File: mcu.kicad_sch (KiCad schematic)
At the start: 31 parts, among them Q22 Q_NPN_BCE, Q23 Q_NPN_BCE, Q24 Q_NPN_BCE, Q25 Q_NPN_BCE, Q26 Q_NPN_BCE, U2 CH32V103C8T6, U3 XTSD01G, Y1 32.768kHz, Y2 16MHz

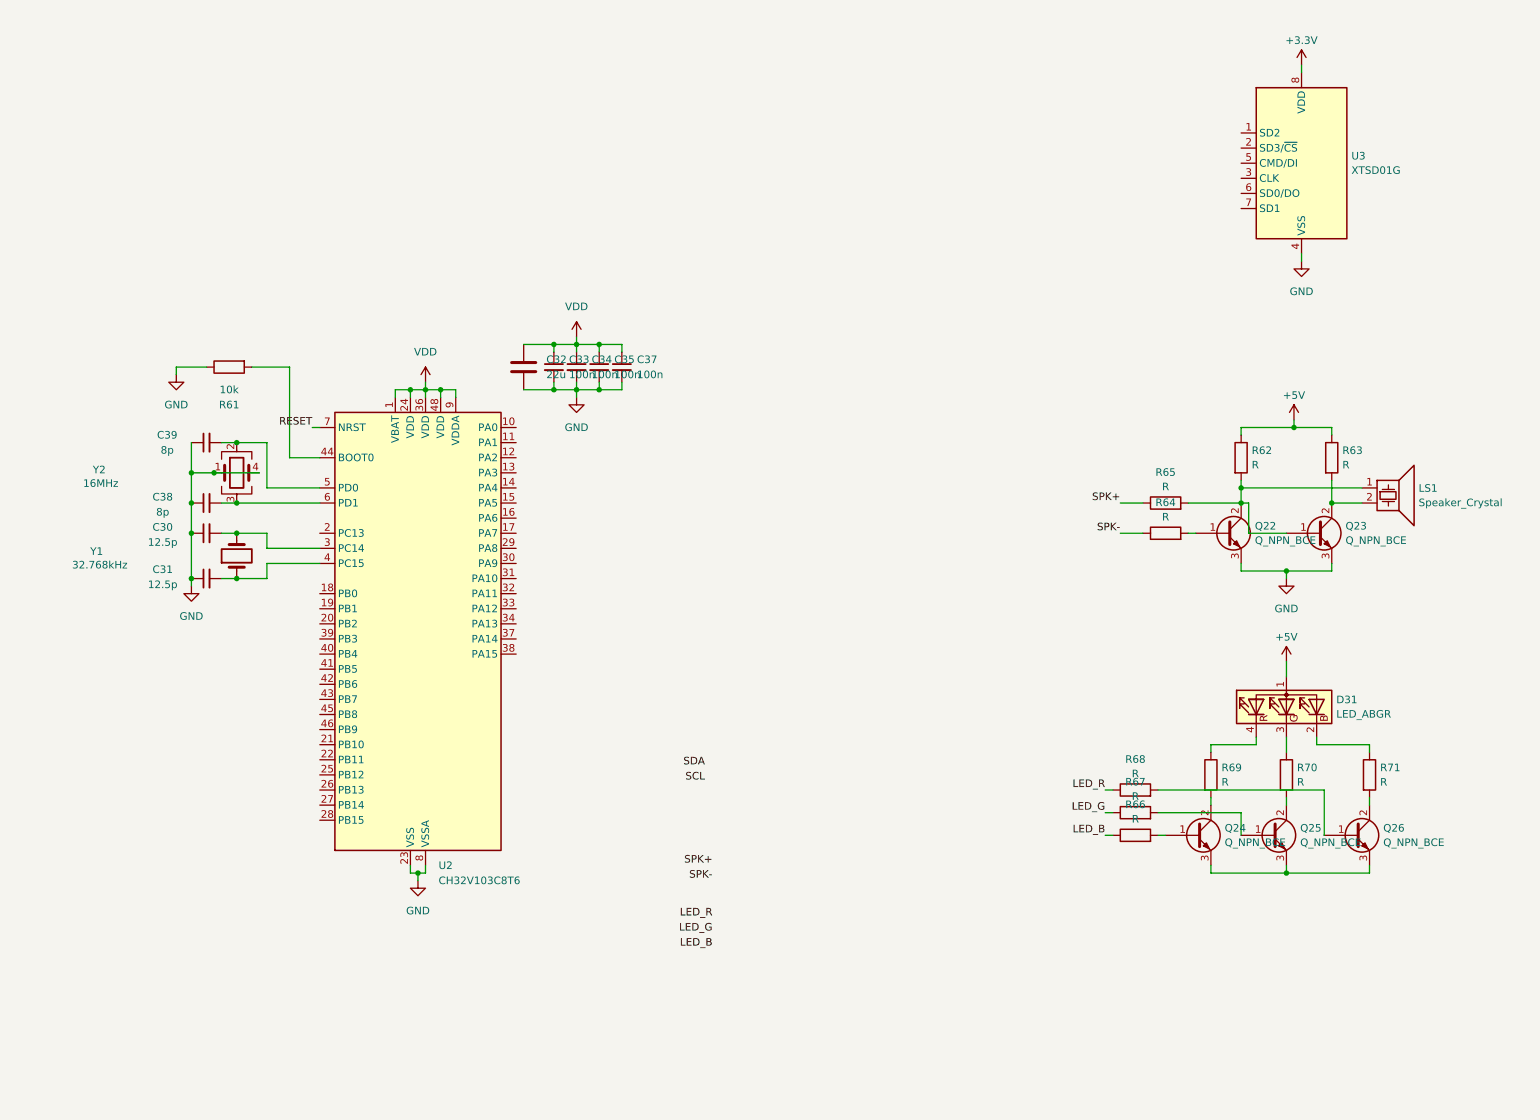
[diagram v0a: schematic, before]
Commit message: fix: 修复commit `38e8c9e`将元器件移动子原理图到造成的位号混乱
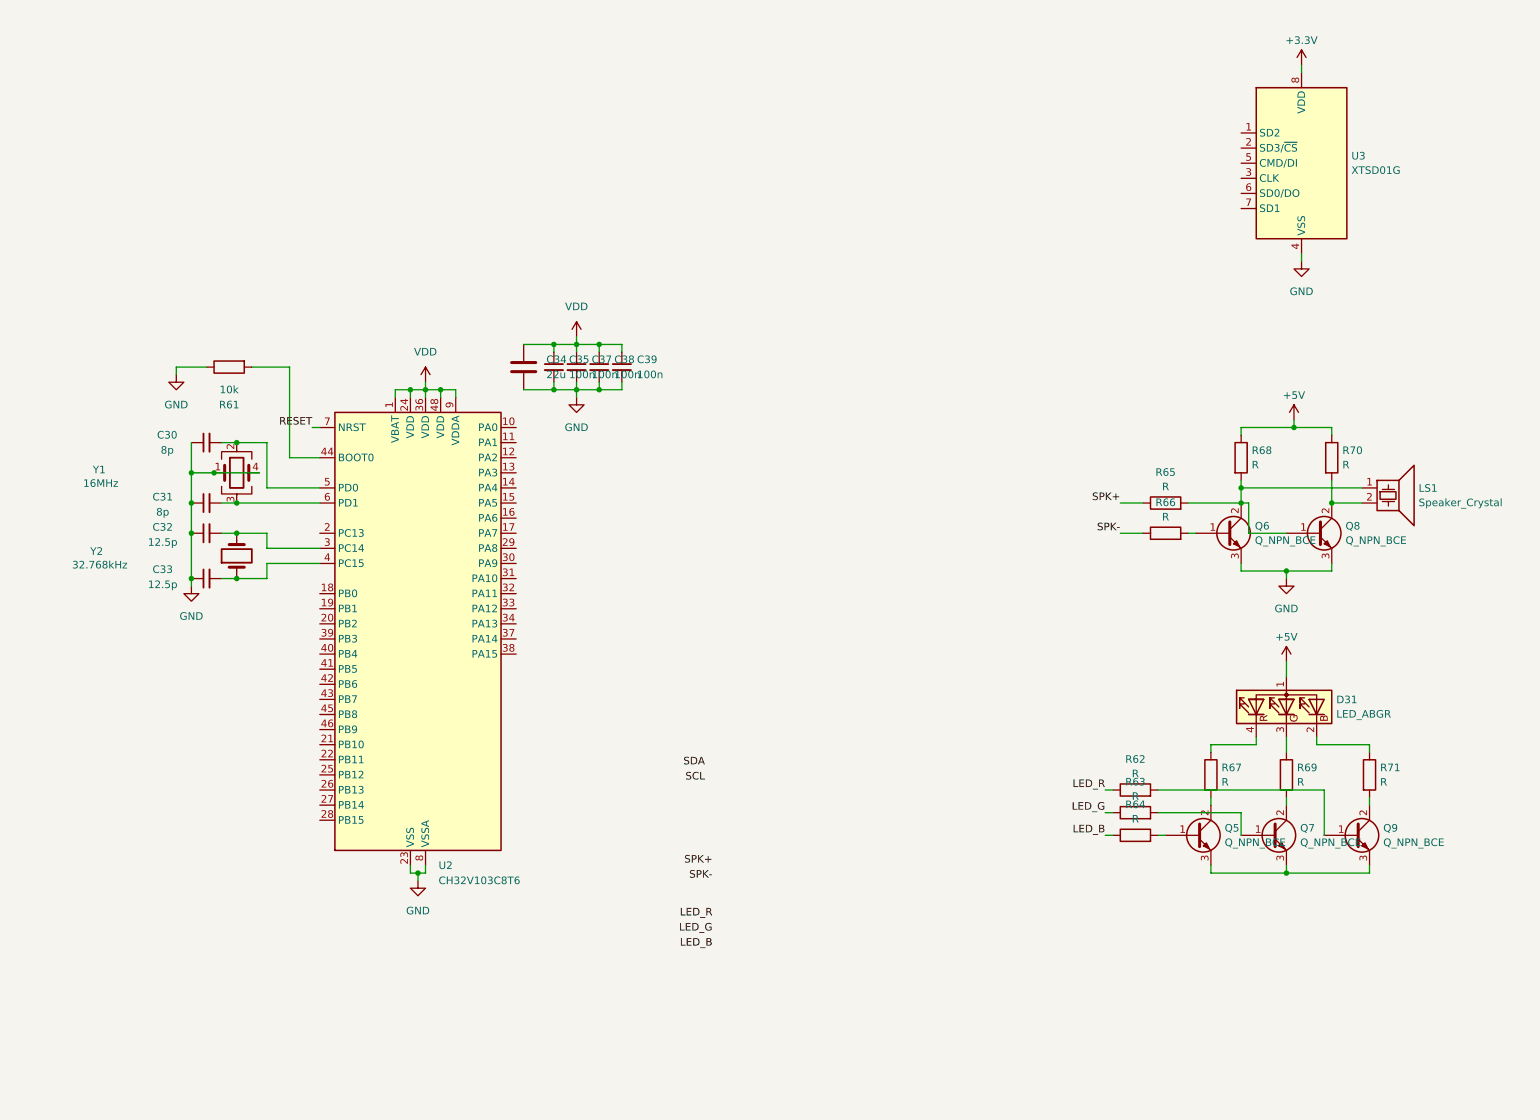
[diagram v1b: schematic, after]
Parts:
- U2: footprint Library:QFP-48_7x7_Pitch0.5mm -> Package_QFP:LQFP-48_7x7mm_P0.5mm
- renumbered C39 to C30, C38 to C31, C30 to C32, C31 to C33, C32 to C34, C33 to C35, C34 to C37, C35 to C38, C37 to C39, Q24 to Q5, Q22 to Q6, Q25 to Q7, Q23 to Q8, Q26 to Q9, R68 to R62, R67 to R63, R66 to R64, R64 to R66, R69 to R67, R62 to R68, R70 to R69, R63 to R70, Y2 to Y1, Y1 to Y2

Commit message: 分配MCU引脚，连接原理图，添加CAN收发器
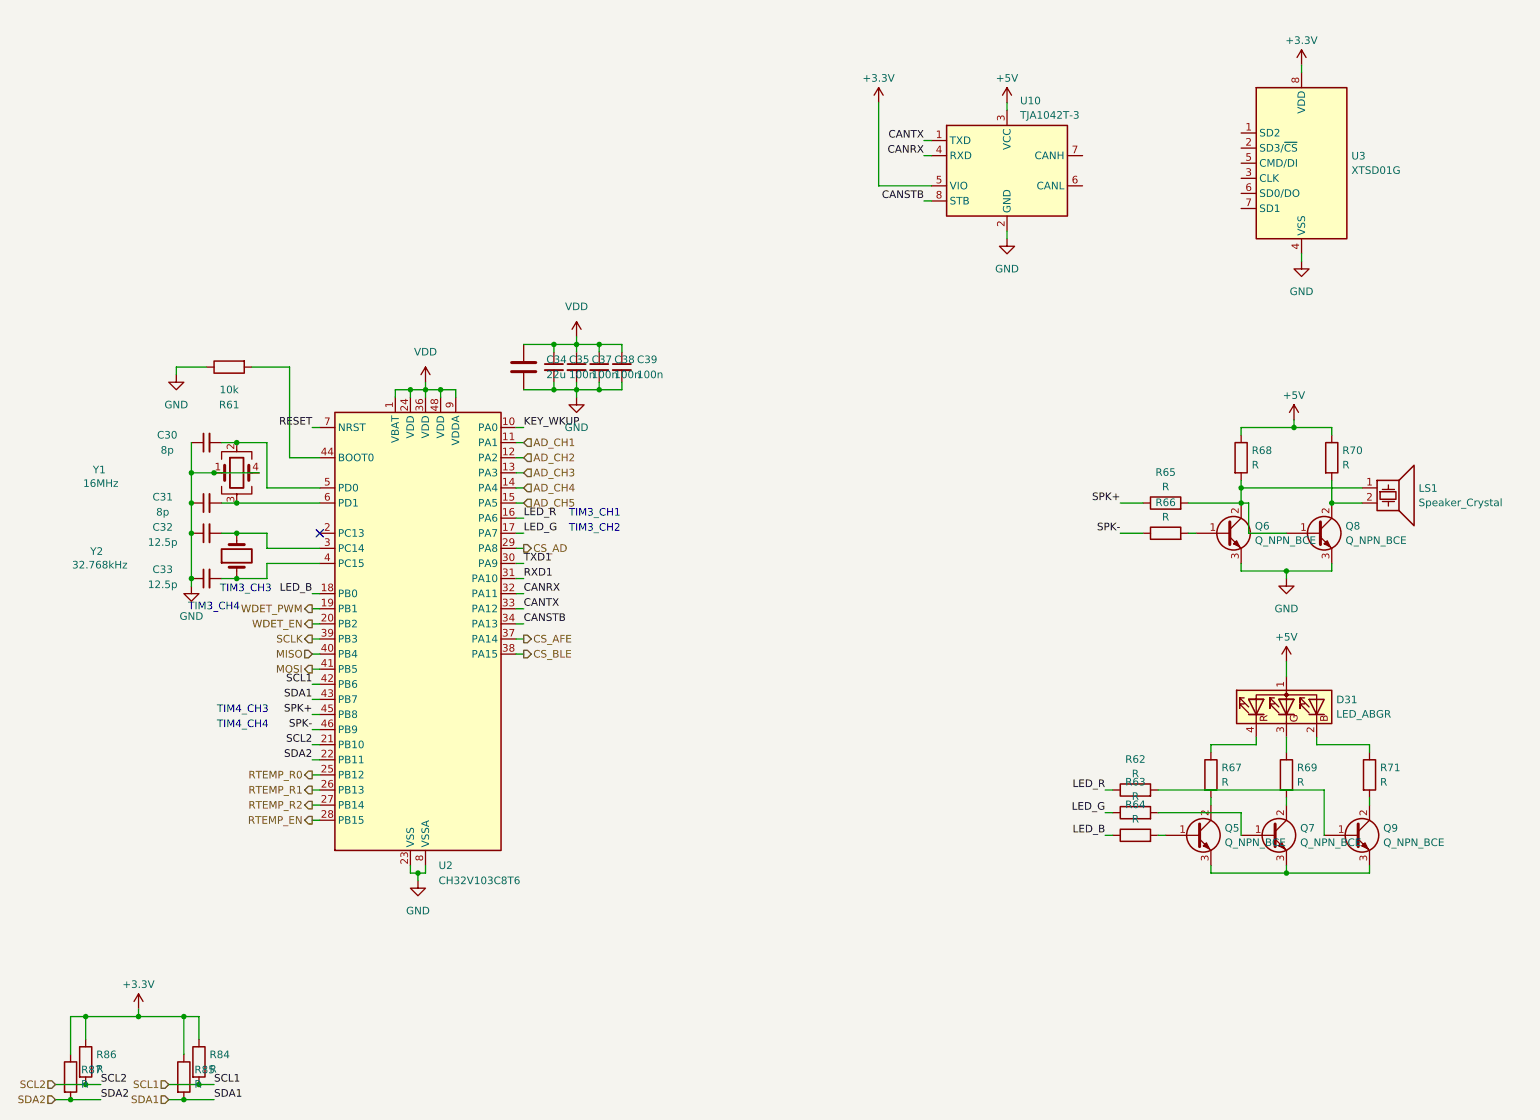
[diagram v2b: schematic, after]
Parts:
- added R84, R85, R86, R87: R, symbol Device:R
- added U10: TJA1042T-3, Package_SO:SOIC-8_3.9x4.9mm_P1.27mm, symbol Interface_CAN_LIN:TJA1042T-3
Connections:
- net +3.3V: now also R84.1, R85.1, R86.1, R87.1, U10.5 (VIO)
- net +5V: now also U10.3 (VCC)
- net GND: now also U10.2 (GND)
- net LED_B: now also U2.18 (PB0)
- net LED_G: now also U2.17 (PA7)
- net LED_R: now also U2.16 (PA6)
- net SPK+: now also U2.45 (PB8)
- net SPK-: now also U2.46 (PB9)
- net KEY_WKUP: now reaches U2.10 (PA0)
- net AD_CH1: now reaches U2.11 (PA1)
- net AD_CH2: now reaches U2.12 (PA2)
- net AD_CH3: now reaches U2.13 (PA3)
- net AD_CH4: now reaches U2.14 (PA4)
- net AD_CH5: now reaches U2.15 (PA5)
- net WDET_PWM: now reaches U2.19 (PB1)
- net WDET_EN: now reaches U2.20 (PB2)
- net SCL2: now reaches U2.21 (PB10)
- net SCL2: now also R86.2
- net SDA2: now reaches U2.22 (PB11)
- net SDA2: now also R87.2
- net RTEMP_R0: now reaches U2.25 (PB12)
- net RTEMP_R1: now reaches U2.26 (PB13)
- net RTEMP_R2: now reaches U2.27 (PB14)
- net RTEMP_EN: now reaches U2.28 (PB15)
- net CS_AD: now reaches U2.29 (PA8)
- net TXD1: now reaches U2.30 (PA9)
- net RXD1: now reaches U2.31 (PA10)
- net CANRX: now reaches U2.32 (PA11)
- net CANRX: now also U10.4 (RXD)
- net CANTX: now reaches U2.33 (PA12)
- net CANTX: now also U10.1 (TXD)
- net CANSTB: now reaches U2.34 (PA13)
- net CANSTB: now also U10.8 (STB)
- net CS_AFE: now reaches U2.37 (PA14)
- net CS_BLE: now reaches U2.38 (PA15)
- net SCLK: now reaches U2.39 (PB3)
- net MISO: now reaches U2.40 (PB4)
- net MOSI: now reaches U2.41 (PB5)
- net SCL1: now reaches U2.42 (PB6)
- net SCL1: now also R84.2
- net SDA1: now reaches U2.43 (PB7)
- net SDA1: now also R85.2
- no-connect marks 0 -> 1
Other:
- note added: "TIM3_CH1"
- note added: "TIM3_CH2"
- note added: "TIM3_CH3"
- note added: "TIM3_CH4"
- note added: "TIM4_CH3"
- note added: "TIM4_CH4"

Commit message: AFE改为PB7170(LQFP-64)，修改原理图，调整元器件布局
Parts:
- R61: footprint Resistor_SMD:R_0201_0603Metric -> Resistor_SMD:R_0402_1005Metric
- Y1: symbol Device:Crystal_GND23 -> Device:Crystal_GND24
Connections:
- net GND: now also Y1.3; no longer Y1.4
- net at C31.2, U2.6 (PD1): now also Y1.4; no longer Y1.3
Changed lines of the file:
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@@
 			)
 		)
-		(property "Footprint" "Resistor_SMD:R_0201_0603Metric"
+		(property "Footprint" "Resistor_SMD:R_0402_1005Metric"
 			(at 50.8 69.342 90)
 			(effects
@@
 	)
 	(symbol
-		(lib_id "Device:Crystal_GND23")
+		(lib_id "Device:Crystal_GND24")
 		(at 52.07 88.9 0)
 		(unit 1)
@@
 			)
 		)
-		(property "Description" "Four pin crystal, GND on pins 2 and 3"
+		(property "Description" "Four pin crystal, GND on pins 2 and 4"
 			(at 52.07 88.9 0)
 			(effects

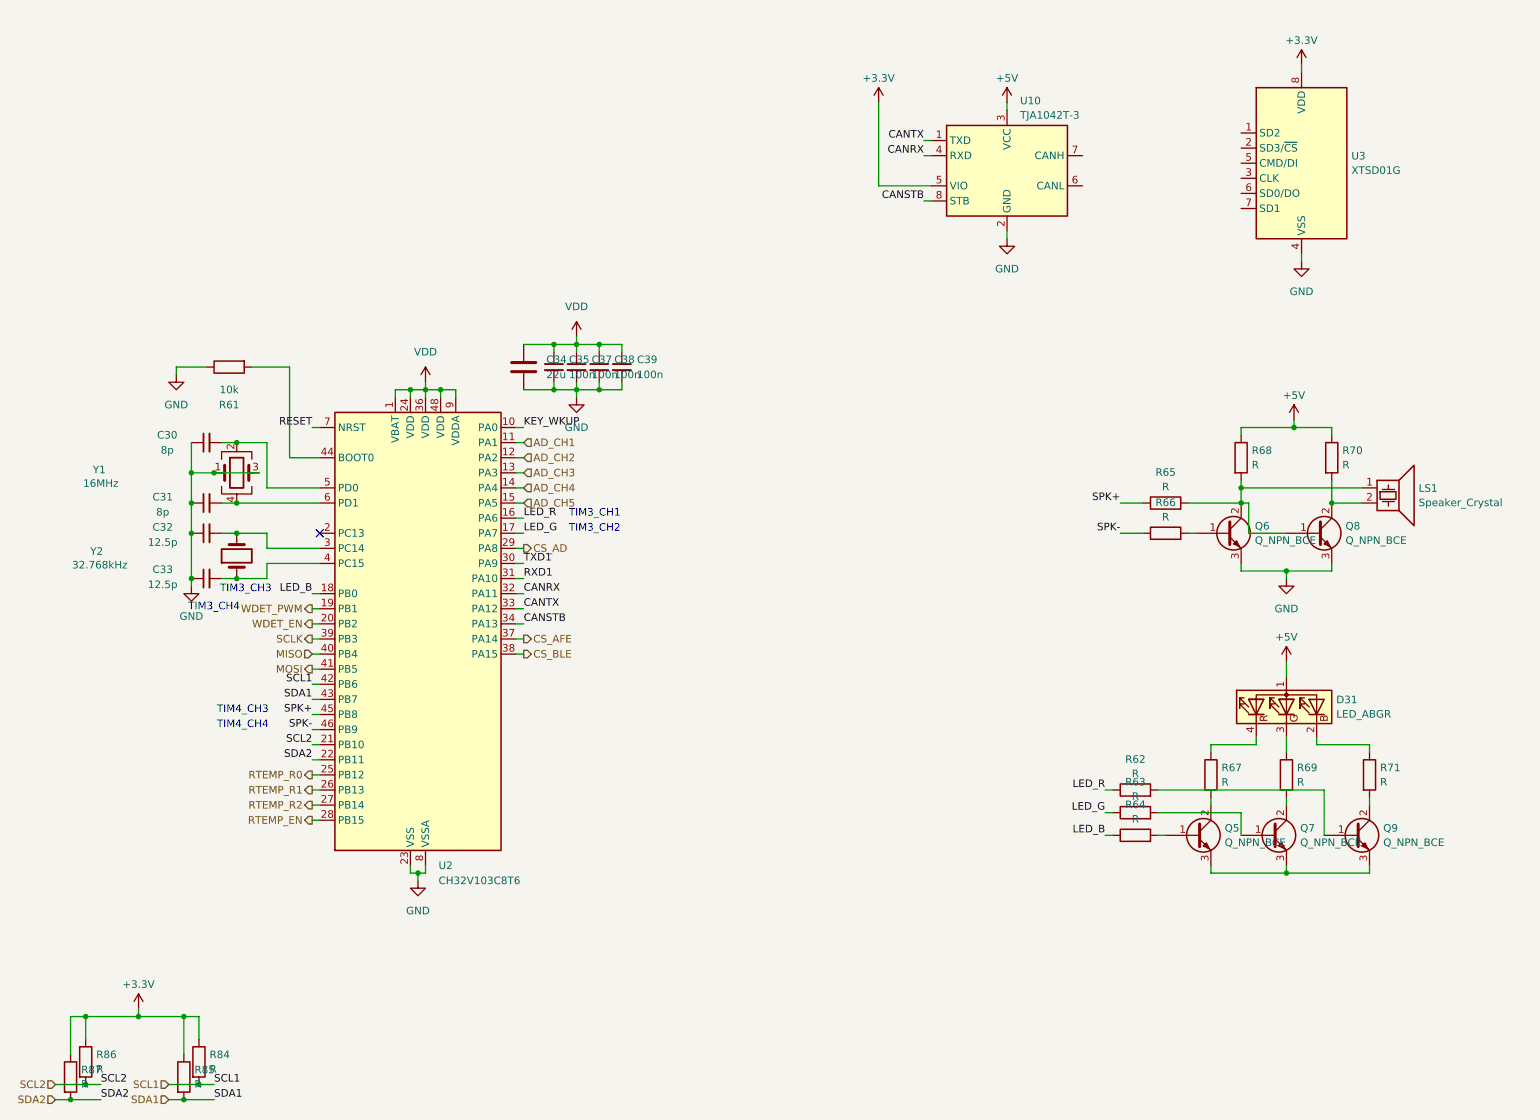
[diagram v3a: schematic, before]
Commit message: 分配封装和在PCB上大致布局
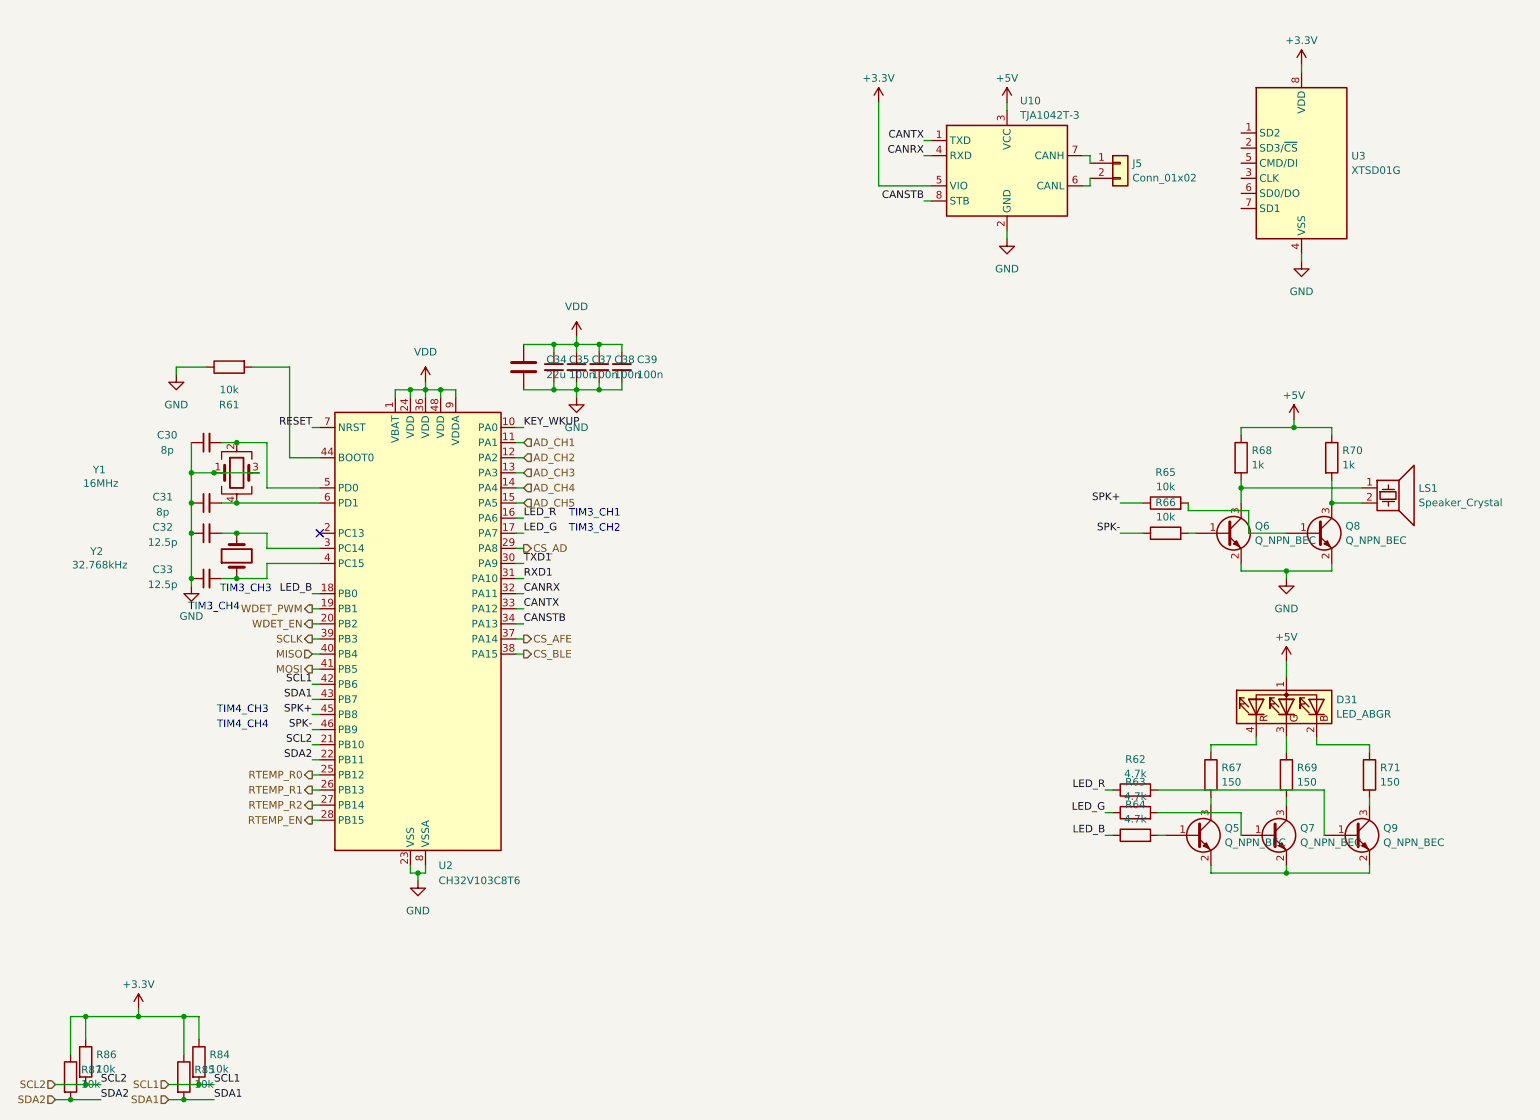
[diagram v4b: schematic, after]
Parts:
- added J5: Conn_01x02, Connector_PinHeader_2.54mm:PinHeader_1x02_P2.54mm_Vertical, symbol Connector_Generic:Conn_01x02
- LS1: footprint (none) -> Connector_PinHeader_2.54mm:PinHeader_1x02_P2.54mm_Vertical
- Q5, Q6, Q7, Q8, Q9: value Q_NPN_BCE -> Q_NPN_BEC; footprint (none) -> Package_TO_SOT_SMD:SOT-23; symbol Device:Q_NPN_BCE -> Device:Q_NPN_BEC
- R62, R63, R64: value R -> 4.7k; footprint (none) -> Resistor_SMD:R_0402_1005Metric
- R65, R66: value R -> 10k; footprint (none) -> Resistor_SMD:R_0402_1005Metric
- R67, R69, R71: value R -> 150; footprint (none) -> Resistor_SMD:R_0603_1608Metric
- R68, R70: value R -> 1k; footprint (none) -> Resistor_SMD:R_0603_1608Metric
- R84, R85, R86, R87: value R -> 10k
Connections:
- net GND: now also Q6.2 (E), Q8.2 (E); no longer Q6.3 (E), Q8.3 (E)
- net at U10.6 (CANL): now also J5.2 (Pin_2)
- net at U10.7 (CANH): now also J5.1 (Pin_1)
- net at Q5.2 (E): now also Q7.2 (E), Q9.2 (E); no longer R67.2
- net at R71.2: now also Q9.3 (C); no longer Q9.2 (C)
- net at LS1.2, R70.2: now also Q8.3 (C); no longer Q8.2 (C)
- net at R69.2: now also Q7.3 (C); no longer Q7.2 (C)
- new net: LS1.1, Q6.3 (C), R68.2
- new net: Q5.3 (C), R67.2
- new net: Q8.1 (B), R65.2
